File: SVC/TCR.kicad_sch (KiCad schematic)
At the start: 23 parts, among them J8 Inductor, Q1 DN2470, Q6 MMBT3906, U1 FODM217D, U4 VOT8121AM, U7 LMC555xM

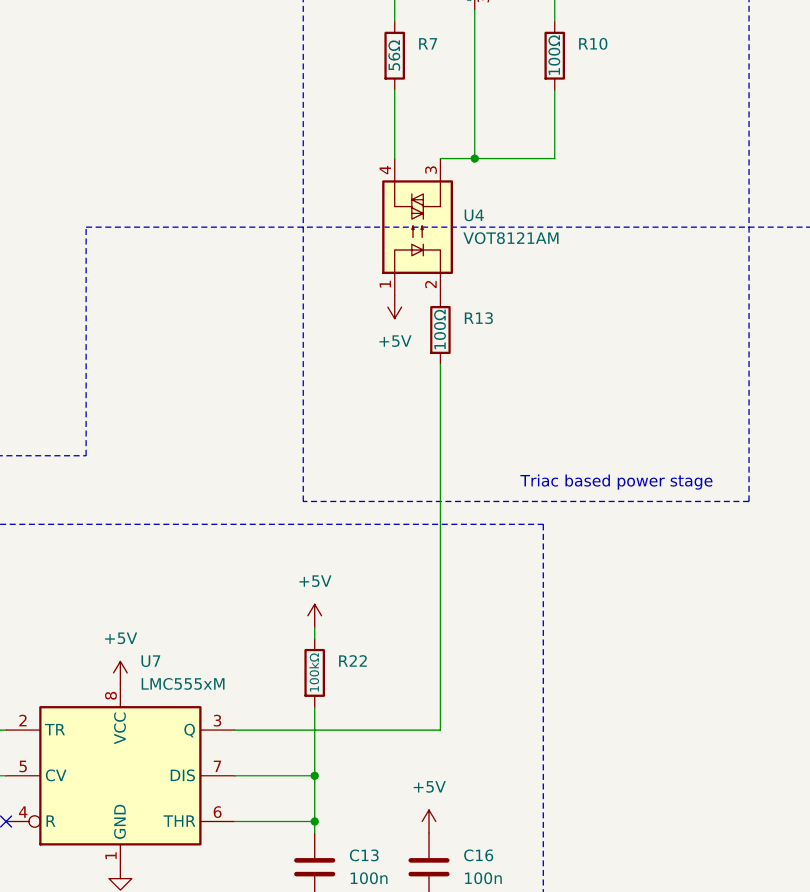
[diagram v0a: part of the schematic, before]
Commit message: did some layout work, minor schematic changes to help with layout
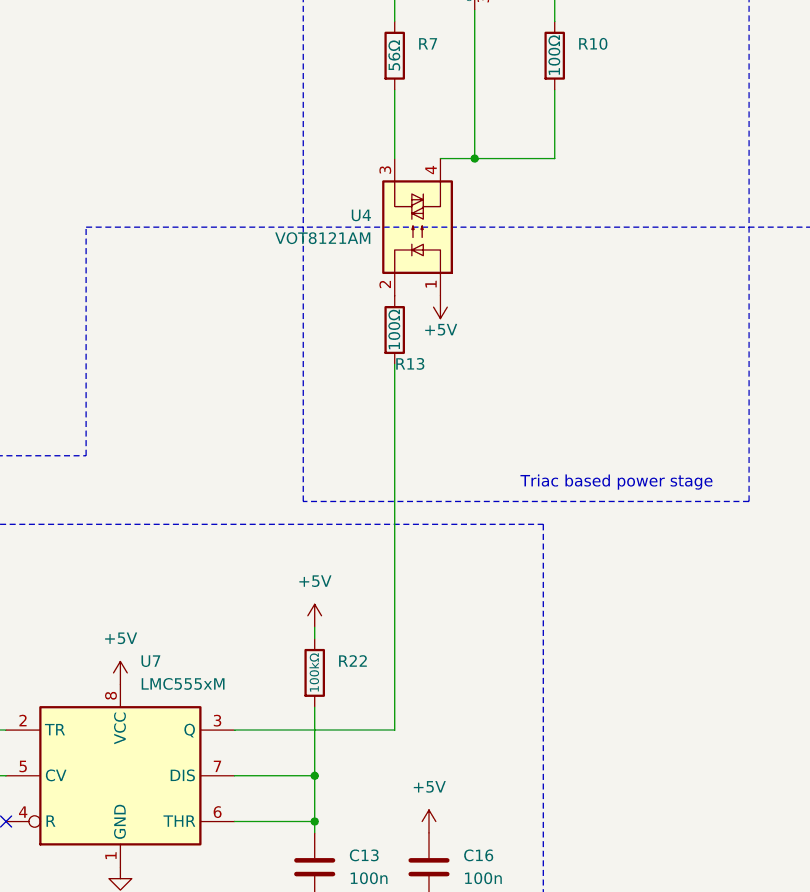
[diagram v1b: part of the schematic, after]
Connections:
- net at R7.2: now also U4.3; no longer U4.4
- net at D9.3 (G), R10.2: now also U4.4; no longer U4.3
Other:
- moved on the sheet: R13, U4
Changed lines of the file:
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@@
     (stroke (width 0) (type default))
   )
-  (wire (pts (xy 154.94 116.84) (xy 177.8 116.84))
+  (wire (pts (xy 154.94 116.84) (xy 172.72 116.84))
     (stroke (width 0) (type default))
   )
@@
     (stroke (width 0) (type default))
   )
-  (wire (pts (xy 177.8 116.84) (xy 177.8 76.2))
+  (wire (pts (xy 172.72 116.84) (xy 172.72 76.2))
     (stroke (width 0) (type default))
   )
@@
     )
   )
-  (symbol (lib_id "power:+5V") (at 172.72 68.58 180) (unit 1)
-    (in_bom yes) (on_board yes) (dnp no) (fields_autoplaced)
-    (property "Reference" "#PWR011" (at 172.72 64.77 0)
-      (effects (font (size 1.27 1.27)) hide)
-    )
-    (property "Value" "+5V" (at 172.72 73.66 0)
-      (effects (font (size 1.27 1.27)))
-    )
-    (property "Footprint" "" (at 172.72 68.58 0)
-      (effects (font (size 1.27 1.27)) hide)
-    )
-    (property "Datasheet" "" (at 172.72 68.58 0)
+  (symbol (lib_id "power:+5V") (at 177.8 68.58 180) (unit 1)
+    (in_bom yes) (on_board yes) (dnp no)
+    (property "Reference" "#PWR011" (at 177.8 64.77 0)
+      (effects (font (size 1.27 1.27)) hide)
+    )
+    (property "Value" "+5V" (at 177.8 72.39 0)
+      (effects (font (size 1.27 1.27)))
+    )
+    (property "Footprint" "" (at 177.8 68.58 0)
+      (effects (font (size 1.27 1.27)) hide)
+    )
+    (property "Datasheet" "" (at 177.8 68.58 0)
       (effects (font (size 1.27 1.27)) hide)
     )
@@
     )
   )
-  (symbol (lib_id "Device:R") (at 177.8 72.39 0) (unit 1)
+  (symbol (lib_id "Device:R") (at 172.72 72.39 0) (unit 1)
     (in_bom yes) (on_board yes) (dnp no)
-    (property "Reference" "R13" (at 180.34 71.12 0)
-      (effects (font (size 1.27 1.27)) (justify left))
-    )
-    (property "Value" "100Ω" (at 177.8 72.39 90)
-      (effects (font (size 1.27 1.27)))
-    )
-    (property "Footprint" "Resistor_SMD:R_1206_3216Metric" (at 176.022 72.39 90)
-      (effects (font (size 1.27 1.27)) hide)
-    )
-    (property "Datasheet" "~" (at 177.8 72.39 0)
+    (property "Reference" "R13" (at 172.72 76.2 0)
+      (effects (font (size 1.27 1.27)) (justify left))
+    )
+    (property "Value" "100Ω" (at 172.72 72.39 90)
+      (effects (font (size 1.27 1.27)))
+    )
+    (property "Footprint" "Resistor_SMD:R_1206_3216Metric" (at 170.942 72.39 90)
+      (effects (font (size 1.27 1.27)) hide)
+    )
+    (property "Datasheet" "~" (at 172.72 72.39 0)
       (effects (font (size 1.27 1.27)) hide)
     )
@@
     )
   )
-  (symbol (lib_id "Relay_SolidState:FODM3053") (at 175.26 60.96 90) (unit 1)
-    (in_bom yes) (on_board yes) (dnp no) (fields_autoplaced)
-    (property "Reference" "U4" (at 180.34 59.69 90)
+  (symbol (lib_id "Relay_SolidState:FODM3053") (at 175.26 60.96 270) (mirror x) (unit 1)
+    (in_bom yes) (on_board yes) (dnp no)
+    (property "Reference" "U4" (at 170.18 59.69 90)
       (effects (font (size 1.27 1.27)) (justify right))
     )
-    (property "Value" "VOT8121AM" (at 180.34 62.23 90)
+    (property "Value" "VOT8121AM" (at 170.18 62.23 90)
       (effects (font (size 1.27 1.27)) (justify right))
     )
-    (property "Footprint" "Package_SO:SOP-4_3.8x4.1mm_P2.54mm" (at 180.34 66.04 0)
+    (property "Footprint" "Package_SO:SOP-4_3.8x4.1mm_P2.54mm" (at 170.18 66.04 0)
       (effects (font (size 1.27 1.27) italic) (justify left) hide)
     )
